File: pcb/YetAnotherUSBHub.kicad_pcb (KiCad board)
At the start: 2 copper layers, 77.6 x 32.6 mm, 24 parts, among them J1 USB_A, J2 USB_A, J3 Micro_SD_Card, J4 USB_C_Receptacle_USB2.0_14P, J5 USB_C_Receptacle_USB2.0_14P, U2 GL823K-HCY04

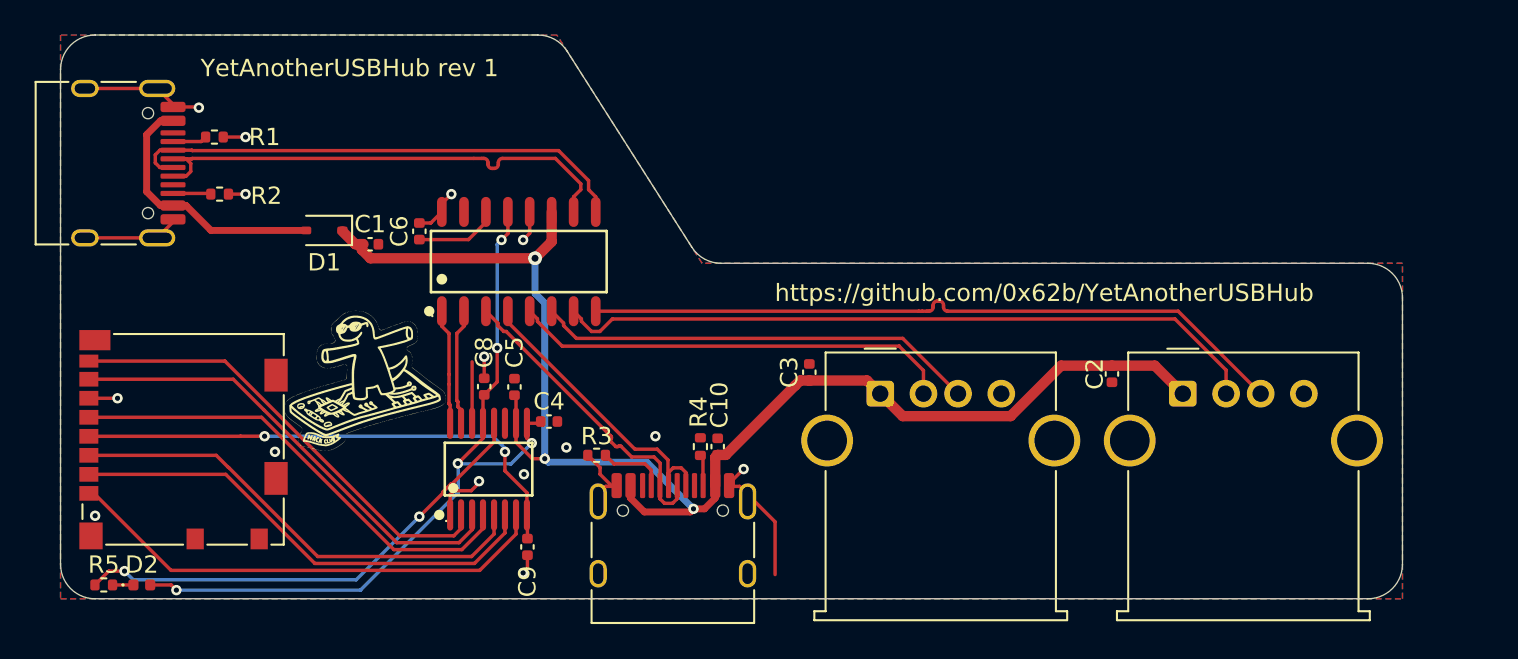
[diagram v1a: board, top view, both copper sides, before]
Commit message: esd protection on pcb
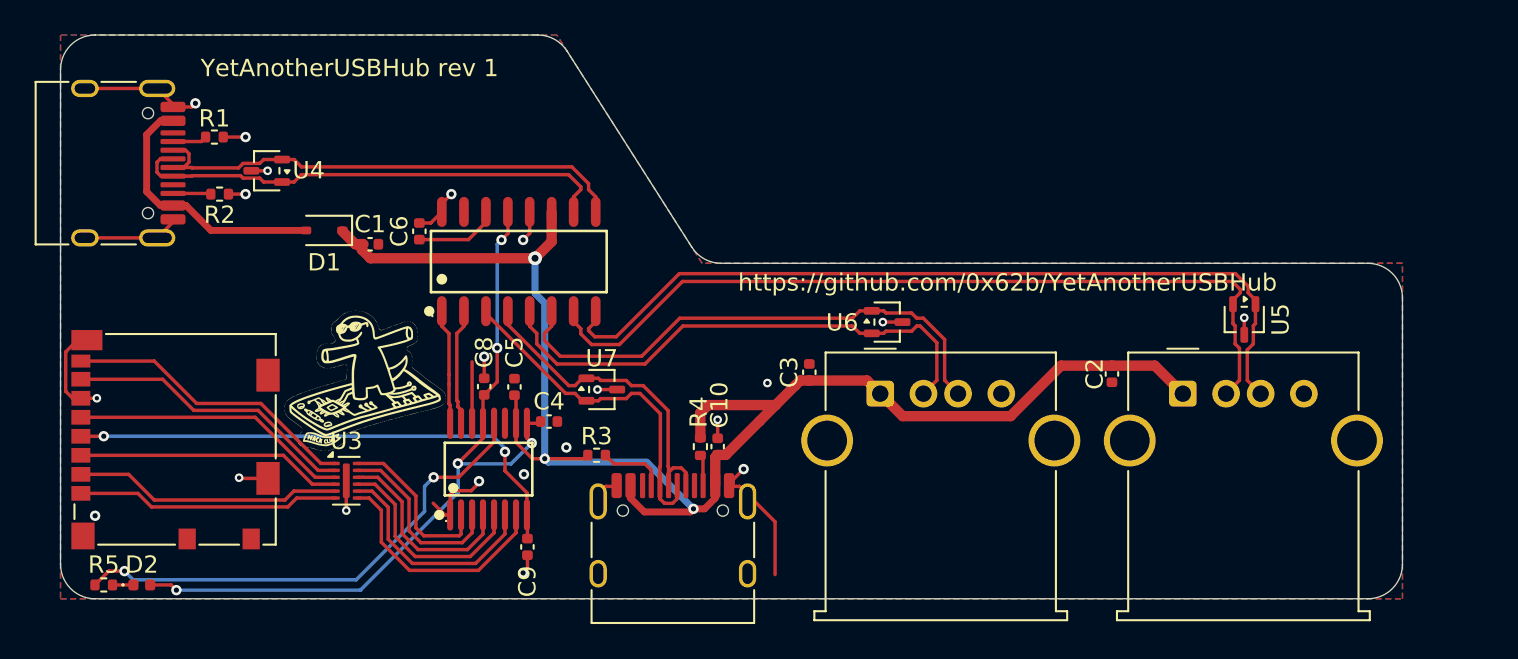
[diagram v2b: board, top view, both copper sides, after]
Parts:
- added U3: TPD6F003, Package_SON:Texas_R-PWSON-N12_EP0.4x2mm, F.Cu at (98.5, 133.7)
- added U4: TPD2E2U06DCK, Package_TO_SOT_SMD:SOT-323_SC-70, F.Cu at (93.9, 115.8)
- added U5: TPD2E2U06DCK, Package_TO_SOT_SMD:SOT-323_SC-70, F.Cu at (150.4, 124.3)
- added U6: TPD2E2U06DCK, Package_TO_SOT_SMD:SOT-323_SC-70, F.Cu at (129.8, 124.5)
- added U7: TPD2E2U06DCK, Package_TO_SOT_SMD:SOT-323_SC-70, F.Cu at (113.3, 128.4)
- R3, R4: value 5.1K -> 56K
- moved J3 0.46 mm to (88.6, 131.3)
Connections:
- J3 pad 1: /DAT2 -> Net-(J3-DAT2)
- J3 pad 2: /DAT3 -> Net-(J3-DAT3/CD)
- J3 pad 3: /CMD -> Net-(J3-CMD)
- J3 pad 5: /CLK -> Net-(J3-CLK)
- J3 pad 7: /DAT0 -> Net-(J3-DAT0)
- J3 pad 8: /DAT1 -> Net-(J3-DAT1)
- R3 pad 2: GND -> /VBUS
- R4 pad 2: GND -> /VBUS
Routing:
- net Net-(J3-DAT1): track 0.00 -> 17.2 mm
- net Net-(J3-DAT0): track 0.00 -> 16.9 mm
- net /DAT1: track 26.4 -> 9.98 mm
- net /DAT0: track 26.9 -> 10.7 mm
- net Net-(J3-CLK): track 0.00 -> 16.2 mm
- net Net-(J3-DAT3/CD): track 0.00 -> 15.6 mm
- net Net-(J3-CMD): track 0.00 -> 15.4 mm
- net /CLK: track 27.0 -> 11.6 mm
- net Net-(J3-DAT2): track 0.00 -> 15.3 mm
- net /CMD: track 27.2 -> 12.3 mm
- net /DAT3: track 27.7 -> 13.2 mm
- net /DAT2: track 28.2 -> 13.9 mm
- net GND: track 41.6 -> 53.4 mm, vias 15 -> 21
- net /VBUS: track 82.6 -> 91.2 mm
- net /USB1_D+: track 41.1 -> 48.3 mm
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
